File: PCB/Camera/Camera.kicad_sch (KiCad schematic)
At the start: 7 parts, among them SW1 SW_Push, SW2 SW_Push, U4 ESP32-WROVER-E

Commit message: PCB changes
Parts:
- removed U4: ESP32-WROVER-E, PCM_Espressif:ESP32-WROVER-E, symbol PCM_Espressif:ESP32-WROVER-E
- added C2: 15 pF, Capacitor_SMD:C_1206_3216Metric_Pad1.33x1.80mm_HandSolder, symbol Device:C
- added C3, C4, C8: 0.1 uF, Capacitor_SMD:C_1206_3216Metric_Pad1.33x1.80mm_HandSolder, symbol Device:C
- added C5: 10 uF, Capacitor_SMD:C_1206_3216Metric_Pad1.33x1.80mm_HandSolder, symbol Device:C
- added C6, C7: 22 uF, Capacitor_SMD:C_1206_3216Metric_Pad1.33x1.80mm_HandSolder, symbol Device:C
- added R3: 1K, Resistor_SMD:R_1206_3216Metric_Pad1.30x1.75mm_HandSolder, symbol Device:R_US
- added R4, R5, R6: 4.7K, Resistor_SMD:R_1206_3216Metric_Pad1.30x1.75mm_HandSolder, symbol Device:R_US
- added U2, U5: ~, PCM_Espressif:ESP32-WROVER-E, symbol Camera_Components:esp32-wrover-e
- added U3: ~, Camera_Components:24-pin-FPC-0.5mm, symbol Camera_Components:Camera_Interface
- added U4: AMS1117-1.2, Package_TO_SOT_SMD:SOT-223-3_TabPin2, symbol Regulator_Linear:AMS1117-1.5
- added U6: AMS1117-2.85, Package_TO_SOT_SMD:SOT-223-3_TabPin2, symbol Regulator_Linear:AMS1117-2.85
- C1: footprint (none) -> Capacitor_SMD:C_1206_3216Metric_Pad1.33x1.80mm_HandSolder
- R1, R2: footprint (none) -> Resistor_SMD:R_1206_3216Metric_Pad1.30x1.75mm_HandSolder
- SW1, SW2: footprint (none) -> Camera_Components:6x6x4.3 SMD button
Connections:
- net 3.3V: now also U1.5 (3.3V), C4.1, C5.1, C8.2, R4.2, R5.1, R6.1, U2.2 (3V3), U3.11 (DOVDD), U4.3 (VI), U5.2 (3V3), U6.3 (VI); no longer U1.4 (3.3V)
- net GNDREF: now also U1.4 (GND), C2.2, C3.1, C4.2, C5.2, C6.1, C7.2, C8.1, R3.2, U2.1 (GND), U2.15 (GND), U2.38 (GND), U3.15 (DGND), U3.2 (AGND), U4.1 (GND), U5.1 (GND), U5.15 (GND), U5.38 (GND), U6.1 (GND); no longer U1.1 (GND)
- net EN renamed B_EN
- net B_EN: now also U2.3 (EN), U5.3 (EN)
- net FLASH RX: no longer names the net of U1.3 (5V)
- net FLASH TX renamed B_RX
- net B_RX: now also U2.34 (RXD0)
- net GPIO0 renamed B_IO0
- net B_IO0: now also U2.25 (IO0), U5.25 (IO0)
- new net 1.2V: C6.2, U3.10 (DVDD), U4.2 (VO)
- new net 2.8V: C7.1, U3.4 (AVDD), U6.2 (VO)
- new net B_TX: U1.1 (BLE_TX), U2.35 (TXD0)
- new net CAM_DATA2: U3.19 (DATA2), U5.14 (IO12)
- new net CAM_DATA3: U3.21 (DATA3), U5.24 (IO2)
- new net CAM_DATA4: U3.22 (DATA4), U5.23 (IO15)
- new net CAM_DATA5: U3.20 (DATA5), U5.16 (IO13)
- new net CAM_DATA6: U3.18 (DATA6), U5.13 (IO14)
- new net CAM_DATA7: U3.16 (DATA7), U5.11 (IO26)
- new net CAM_DATA8: U3.14 (DATA8), U5.10 (IO25)
- new net CAM_DATA9: U3.12 (DATA9), U5.8 (IO32)
- new net CAM_HREF: U3.9 (HREF), U5.7 (IO35)
- new net CAM_PCLK: C2.1, U3.17 (PCLK), U5.12 (IO27)
- new net CAM_PWDN: R3.1, U3.8 (PWDN)
- new net CAM_RESET: C3.2, R4.1, U3.6 (RESETB)
- new net CAM_SIOC: R6.2, U3.5 (SIOC), U5.5 (SENSOR_VN)
- new net CAM_SIOD: R5.2, U3.3 (SIOD), U5.4 (SENSOR_VP)
- new net CAM_VSYNC: U3.7 (VSYNC), U5.6 (IO34)
- new net CAM_XCLK: U3.13 (XCLK), U5.9 (IO33)
- new net IPC_RX: U2.29 (IO5), U5.28 (IO17)
- new net IPC_TX: U2.28 (IO17), U5.29 (IO5)
- new net W_RX: U1.6 (WIFI_RX), U5.34 (RXD0)
- new net W_TX: U1.7 (WIFI_TX), U5.35 (TXD0)
- no-connect marks 1 -> 14
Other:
- note added: "1.0"
- note added: "Camera"
- moved on the sheet: C1, R1, R2, SW1, SW2

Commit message: PCB changes
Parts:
- removed C6, C7: 22 uF, Capacitor_SMD:C_1206_3216Metric_Pad1.33x1.80mm_HandSolder, symbol Device:C
- removed U4: AMS1117-1.2, Package_TO_SOT_SMD:SOT-223-3_TabPin2, symbol Regulator_Linear:AMS1117-1.5
- removed U6: AMS1117-2.85, Package_TO_SOT_SMD:SOT-223-3_TabPin2, symbol Regulator_Linear:AMS1117-2.85
- added C10, C11: 1 uF, Capacitor_SMD:C_1206_3216Metric_Pad1.33x1.80mm_HandSolder, symbol Device:C
- added D1: LED, Camera_Components:vibration motor, symbol Device:LED
- added Q1, Q2: S8050, Camera_Components:transistor, symbol Transistor_BJT:S8050
- added R7, R8: 4.7K, Resistor_SMD:R_1206_3216Metric_Pad1.30x1.75mm_HandSolder, symbol Device:R_US
- added U10, U8: ~, Camera_Components:XC6206, symbol Camera_Components:XC6206
- added U7: ~, Camera_Components:vibration motor, symbol Camera_Components:Vibration_Motor
- renumbered SW2 to BOOT1, U3 to CAMERA1, SW1 to RESET1
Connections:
- net 1.2V: now also C10.2, U8.2 (VOUT)
- net 2.8V: now also C11.2, U10.2 (VOUT)
- net 3.3V: now also Q1.3 (C), Q2.3 (C), R7.2, U10.3 (VIN), U8.3 (VIN)
- net GNDREF: now also C10.1, C11.1, D1.1 (K), U10.1 (VSS), U7.2 (GND), U8.1 (VSS)
- net V_CTRL: now reaches U2.13 (IO14)
- net V_CTRL: now also Q1.2 (B), R7.1
- net LED_CTRL: now reaches U2.8 (IO32)
- net LED_CTRL: now also Q2.2 (B)
- new net: D1.2 (A), R8.1
- new net: Q2.1 (E), R8.2
- new net: Q1.1 (E), U7.1 (PWR)
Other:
- note added: "1.2V"
- note added: "2.8V"
- moved on the sheet: C3, C8, R4, U5

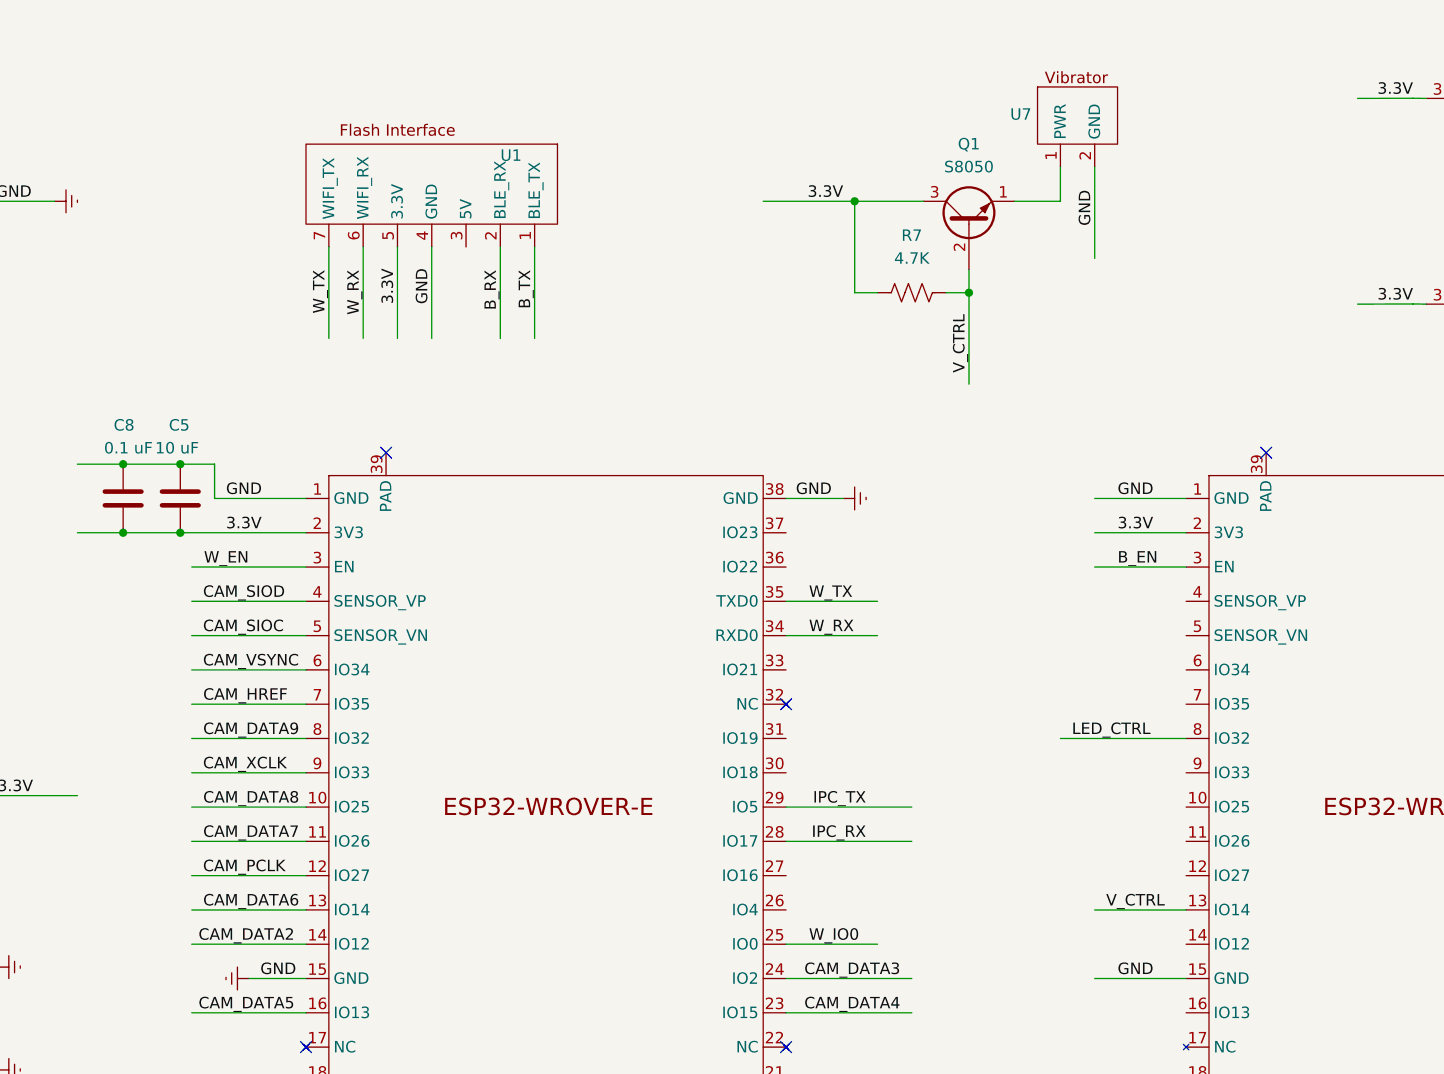
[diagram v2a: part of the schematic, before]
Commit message: Added a BUTTON hell yeah
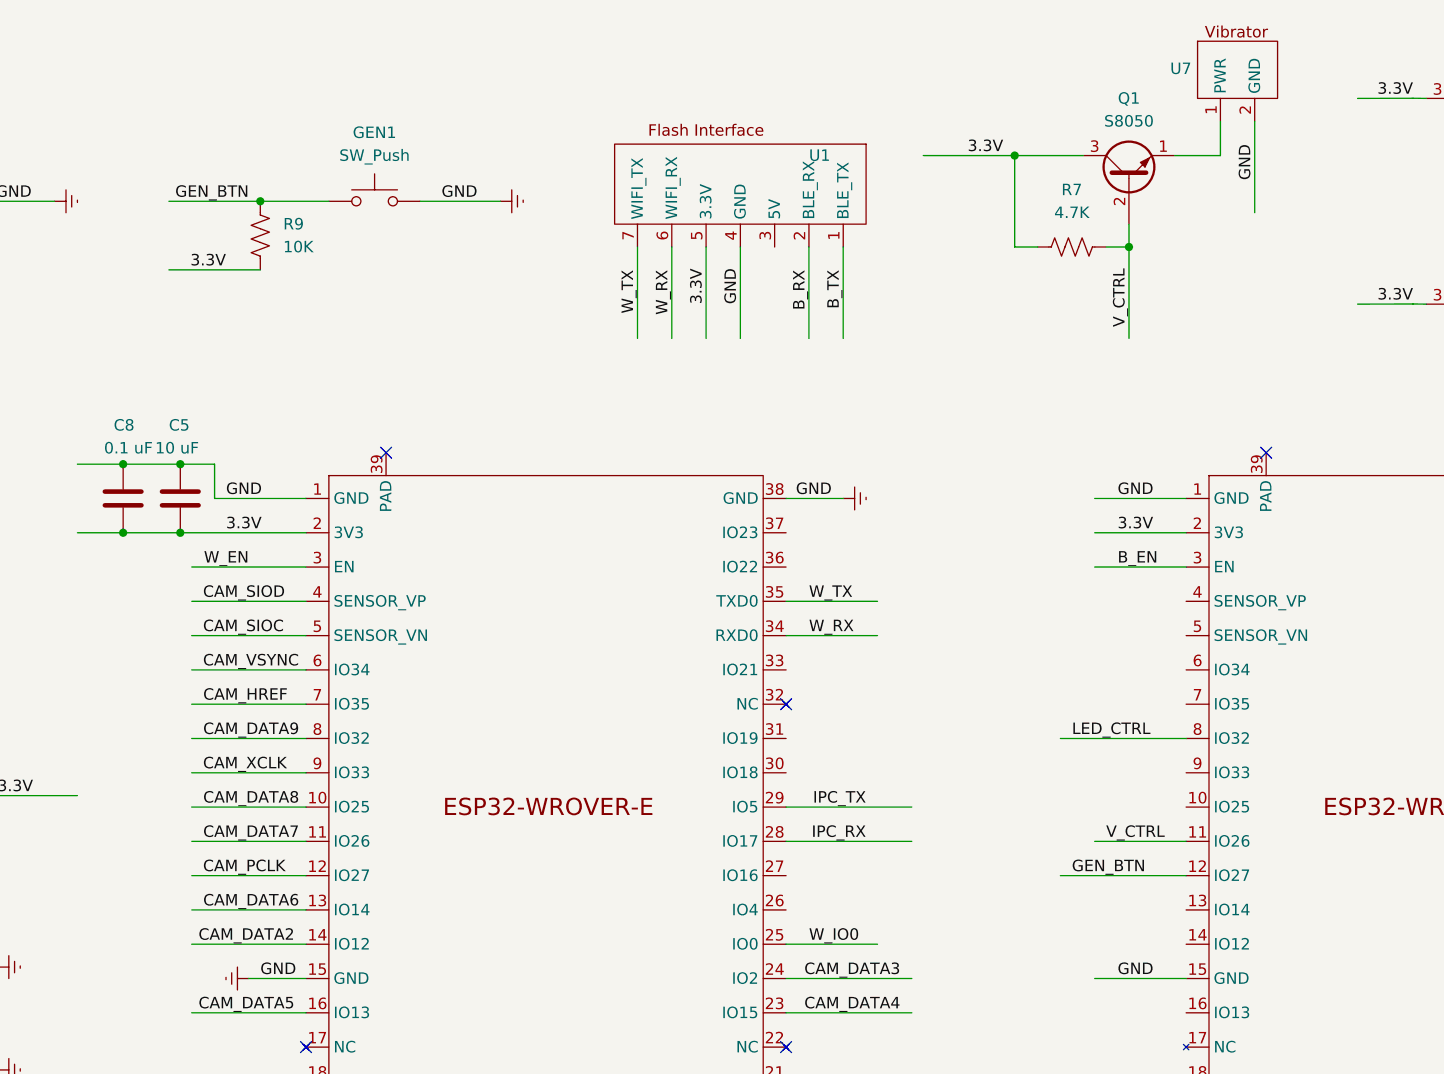
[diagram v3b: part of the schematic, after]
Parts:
- added GEN1: SW_Push, Camera_Components:6x6x4.3 SMD button, symbol Switch:SW_Push
- added R9: 10K, Resistor_SMD:R_1206_3216Metric_Pad1.30x1.75mm_HandSolder, symbol Device:R_US
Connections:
- net 3.3V: now also R9.2
- net GNDREF: now also GEN1.2
- net V_CTRL: now also U2.11 (IO26); no longer U2.13 (IO14)
- net GEN_BTN: now reaches U2.12 (IO27)
- net GEN_BTN: now also GEN1.1, R9.1
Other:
- moved on the sheet: Q1, R7, U1, U7

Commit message: integration stuff
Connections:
- net CAM_DATA6: now also U5.7 (IO35); no longer U5.13 (IO14)
- net CAM_DATA7: now also U5.6 (IO34); no longer U5.11 (IO26)
- net CAM_DATA8: now also U5.5 (SENSOR_VN); no longer U5.10 (IO25)
- net CAM_DATA9: now also U5.4 (SENSOR_VP); no longer U5.8 (IO32)
- net CAM_HREF: now also U5.11 (IO26); no longer U5.7 (IO35)
- net CAM_PCLK: now also U5.13 (IO14); no longer U5.12 (IO27)
- net CAM_SIOC: now also U5.9 (IO33); no longer U5.5 (SENSOR_VN)
- net CAM_SIOD: now also U5.8 (IO32); no longer U5.4 (SENSOR_VP)
- net CAM_VSYNC: now also U5.10 (IO25); no longer U5.6 (IO34)
- net CAM_XCLK: now also U5.12 (IO27); no longer U5.9 (IO33)
